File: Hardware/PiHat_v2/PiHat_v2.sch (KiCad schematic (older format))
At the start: 8 parts, among them P1 CONN_02X20, P2 CONN_01X02

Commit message: Correct EEPROM Schematic - Add Pin Numbers
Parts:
- PP1: footprint (none) -> Measurement_Points:Test_Point_2Pads
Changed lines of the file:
@@
 $EndComp
 $Comp
-L +3.3V #PWR1
+L +3.3V #PWR01
 U 1 1 588858F3
 P 1050 900
-F 0 "#PWR1" H 1050 750 50  0001 C CNN
+F 0 "#PWR01" H 1050 750 50  0001 C CNN
 F 1 "+3.3V" H 1050 1040 50  0000 C CNN
 F 2 "" H 1050 900 50  0000 C CNN
@@
 $EndComp
 $Comp
-L +5V #PWR3
+L +5V #PWR02
 U 1 1 58885909
 P 1700 900
-F 0 "#PWR3" H 1700 750 50  0001 C CNN
+F 0 "#PWR02" H 1700 750 50  0001 C CNN
 F 1 "+5V" H 1700 1040 50  0000 C CNN
 F 2 "" H 1700 900 50  0000 C CNN
@@
 $EndComp
 $Comp
-L GND #PWR4
+L GND #PWR03
 U 1 1 58885944
 P 1700 3100
-F 0 "#PWR4" H 1700 2850 50  0001 C CNN
+F 0 "#PWR03" H 1700 2850 50  0001 C CNN
 F 1 "GND" H 1700 2950 50  0000 C CNN
 F 2 "" H 1700 3100 50  0000 C CNN
@@
 $EndComp
 $Comp
-L GND #PWR2
+L GND #PWR04
 U 1 1 58885AD1
 P 1100 3100
-F 0 "#PWR2" H 1100 2850 50  0001 C CNN
+F 0 "#PWR04" H 1100 2850 50  0001 C CNN
 F 1 "GND" H 1100 2950 50  0000 C CNN
 F 2 "" H 1100 3100 50  0000 C CNN
@@
 ID_SD
 $Comp
-L GND #PWR5
+L GND #PWR05
 U 1 1 58887CDD
 P 2700 2300
-F 0 "#PWR5" H 2700 2050 50  0001 C CNN
+F 0 "#PWR05" H 2700 2050 50  0001 C CNN
 F 1 "GND" H 2700 2150 50  0000 C CNN
 F 2 "" H 2700 2300 50  0000 C CNN
@@
 $EndComp
 $Comp
-L +3.3V #PWR8
+L +3.3V #PWR06
 U 1 1 58887DFD
 P 3750 1250
-F 0 "#PWR8" H 3750 1100 50  0001 C CNN
+F 0 "#PWR06" H 3750 1100 50  0001 C CNN
 F 1 "+3.3V" H 3750 1390 50  0000 C CNN
 F 2 "" H 3750 1250 50  0000 C CNN
@@
 $EndComp
 $Comp
-L GND #PWR6
+L GND #PWR07
 U 1 1 58887E15
 P 3350 1500
-F 0 "#PWR6" H 3350 1250 50  0001 C CNN
+F 0 "#PWR07" H 3350 1250 50  0001 C CNN
 F 1 "GND" H 3350 1350 50  0000 C CNN
 F 2 "" H 3350 1500 50  0000 C CNN
@@
 $EndComp
 $Comp
-L GND #PWR7
+L GND #PWR08
 U 1 1 58887E2F
 P 3700 2900
-F 0 "#PWR7" H 3700 2650 50  0001 C CNN
+F 0 "#PWR08" H 3700 2650 50  0001 C CNN
 F 1 "GND" H 3700 2750 50  0000 C CNN
 F 2 "" H 3700 2900 50  0000 C CNN
@@
 F 0 "PP1" H 3460 2770 50  0000 C CNN
 F 1 "horizTest" H 3450 2520 50  0000 C CNN
-F 2 "" H 3310 2700 50  0000 C CNN
+F 2 "Measurement_Points:Test_Point_2Pads" H 3310 2700 50  0001 C CNN
 F 3 "" H 3310 2700 50  0000 C CNN
 	1    3450 2650

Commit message: Rough Sketch of Schematic and all Footprints Complete
* I've completed a first draft of the schematic, and verified that all
parts have a footprint.
* Next steps include routing the PCB, verifying the designs, and
including any changes.
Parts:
- added LED1: Led_RGB_CA, LEDs:LED_Cree-PLCC4, symbol Led_RGB_CA
- added P3: CONN_01X08, Pin_Headers:Pin_Header_Straight_1x08_Pitch2.54mm, symbol CONN_01X08
- added R4, R5, R6: R, Resistors_SMD:R_0805_HandSoldering, symbol R
- added S1: Piezo, .pretty:PKM13EPYH, symbol Piezo
- added aux1, aux2, aux3, aux4: CONN_01X02, Connectors_Molex:Molex_KK-6410-02_02x2.54mm_Straight, symbol CONN_01X02
- added temp1: LM75BD, Housings_SOIC:SOIC-8_3.9x4.9mm_Pitch1.27mm, symbol LM75BD
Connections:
- wire segments 66 -> 94
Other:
- note added: "3x4 Keypad"
- note added: "Aux Switch Connections"
- note added: "Piezo Buzzer"
- note added: "RGB Led - Common Anode"
- note added: "i2c Temperature Sensor"
- moved on the sheet: C1, ID_EEPROM1, P1, P2, PP1, R1, R2, R3

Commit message: Merge branch 'clemsonMakerspace/devel' into devel
# Conflicts:
#	Software/scan_key/AuthenticationSQL.py
#	Software/scan_key/main.py
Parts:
- removed LED1: Led_RGB_CA, LEDs:LED_Cree-PLCC4, symbol Led_RGB_CA
- removed R4, R5, R6: R, Resistors_SMD:R_0805_HandSoldering, symbol R
- added C2: 100n, Capacitors_SMD:C_0805_HandSoldering, symbol C
- added D1: D_Schottky, .pretty:Schottky_Diode, symbol D_Schottky
- added P4: Neo_LED_RGB_IC, .pretty:Neo_RGB_LED, symbol Neo_LED_RGB_IC
- added aux5: CONN_01X02, Connectors_Molex:Molex_KK-6410-02_02x2.54mm_Straight, symbol CONN_01X02
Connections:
- wire segments 94 -> 93
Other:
- note added: "RGB Neopixel Led - Integrated IC"
- note removed: "RGB Led - Common Anode"
- moved on the sheet: C1, ID_EEPROM1, P1, P2, P3, PP1, R1, R2, R3, S1, aux1, aux2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

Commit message: Merge remote-tracking branch 'refs/remotes/clemsonMakerspace/devel' into devel
# Conflicts:
#	Hardware/PiHat_v2/.pretty/Neo_RGB_LED.kicad_mod
#	Hardware/PiHat_v2/PiHat_v2.kicad_pcb
#	Hardware/PiHat_v2/PiHat_v2.kicad_pcb-bak
#	Hardware/PiHat_v2/PiHat_v2.net
#	Hardware/PiHat_v2/PiHat_v2.pro
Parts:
- removed D1: D_Schottky, .pretty:Schottky_Diode, symbol D_Schottky
- added ATMEGA1: ATMEGA328P-A, .pretty:ATMEGA328P, symbol ATMEGA328P-A
- added C3, C4: 20p, Capacitors_THT:C_Disc_D5.0mm_W2.5mm_P2.50mm, symbol C
- added OSC1: 16 MHz Crystal, Crystals:Resonator-2pin_w10.0mm_h5.0mm, symbol Piezo
- added R4: 1K, Resistors_SMD:R_0805_HandSoldering, symbol R
- added R5: 10K, Resistors_SMD:R_0805_HandSoldering, symbol R
- P3: footprint Pin_Headers:Pin_Header_Straight_1x08_Pitch2.54mm -> .pretty:Keypad_Ethernet
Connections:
- net labels added: ADC6, PB1, PD3, PD6, UART_RXD, UART_TXD
- net labels removed: GPIO14, GPIO15
- wire segments 93 -> 120
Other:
- note added: "Second Microcontroller\n"
- moved on the sheet: C1, ID_EEPROM1, P2, PP1, R1, R2, R3, S1, temp1

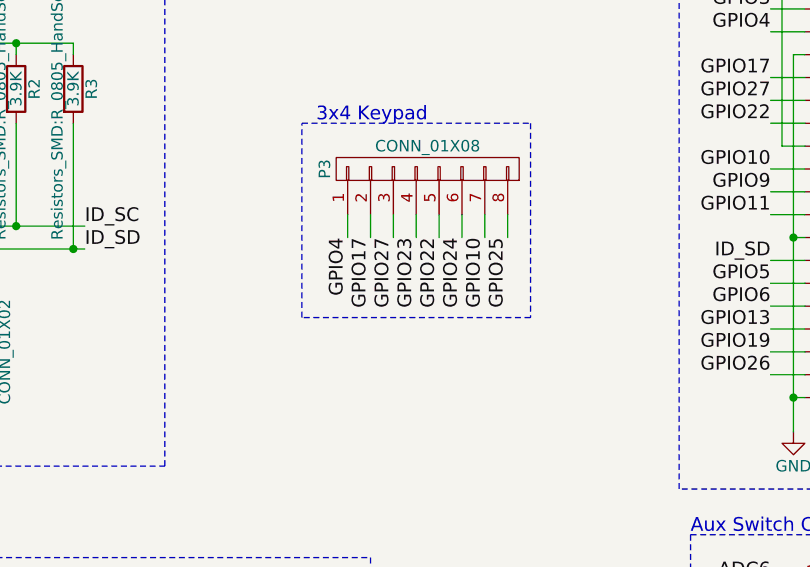
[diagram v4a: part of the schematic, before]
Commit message: Fixed my branch and moved ethernet port
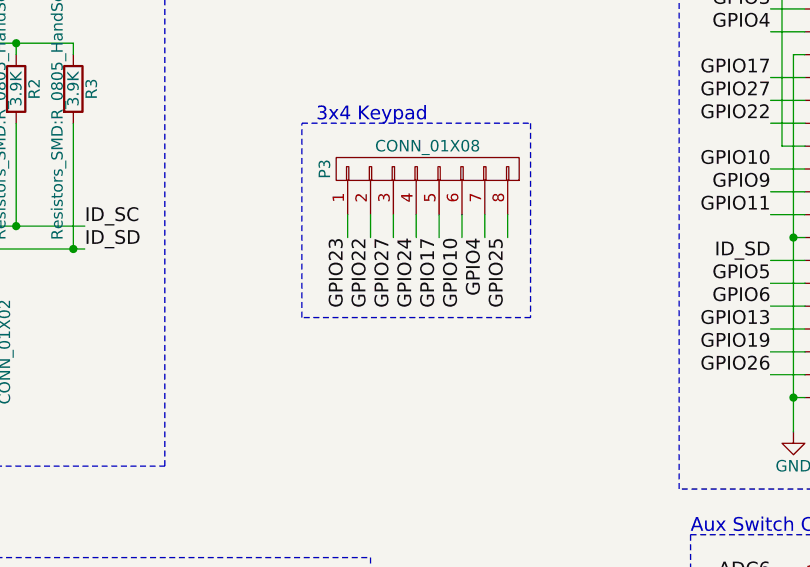
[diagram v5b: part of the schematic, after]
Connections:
- net GPIO10: now also P3.6 (P6); no longer P3.7 (P7)
- net GPIO17: now also P3.5 (P5); no longer P3.2 (P2)
- net GPIO22: now also P3.2 (P2); no longer P3.5 (P5)
- net GPIO23: now also P3.1 (P1); no longer P3.4 (P4)
- net GPIO24: now also P3.4 (P4); no longer P3.6 (P6)
- net GPIO4: now also P3.7 (P7); no longer P3.1 (P1)
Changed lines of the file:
@@
 Text Label 2150 1400 2    60   ~ 0
 PB1
-Text Label 6550 2950 3    60   ~ 0
+Text Label 7150 2950 3    60   ~ 0
 GPIO4
-Text Label 6650 2950 3    60   ~ 0
+Text Label 6950 2950 3    60   ~ 0
 GPIO17
 Text Label 6750 2950 3    60   ~ 0
 GPIO27
-Text Label 6850 2950 3    60   ~ 0
+Text Label 6550 2950 3    60   ~ 0
 GPIO23
 Wire Wire Line
 	7250 2850 7250 2950
-Text Label 6950 2950 3    60   ~ 0
+Text Label 6650 2950 3    60   ~ 0
 GPIO22
+Text Label 6850 2950 3    60   ~ 0
+GPIO24
 Text Label 7050 2950 3    60   ~ 0
-GPIO24
-Text Label 7150 2950 3    60   ~ 0
 GPIO10
 Text Label 7250 2950 3    60   ~ 0

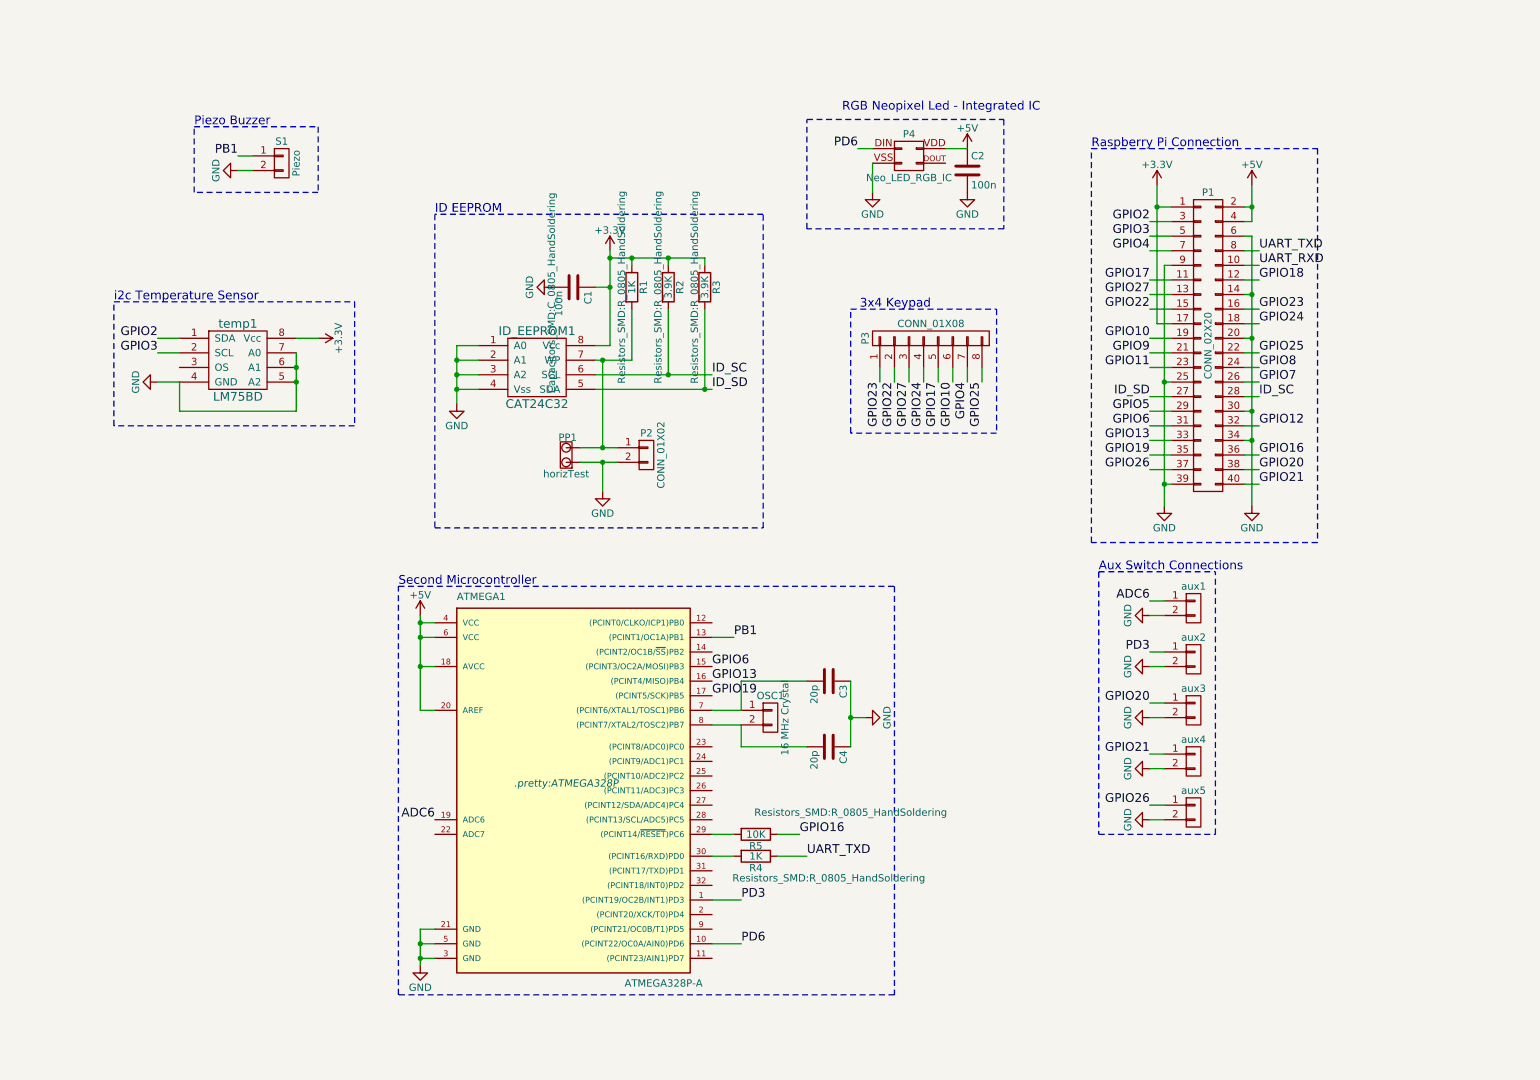
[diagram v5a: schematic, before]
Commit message: Schematic for Neopixel Chain & ISP Program Header
I've chained 5 Neopixels and added an ISP header for the ATMEGA.
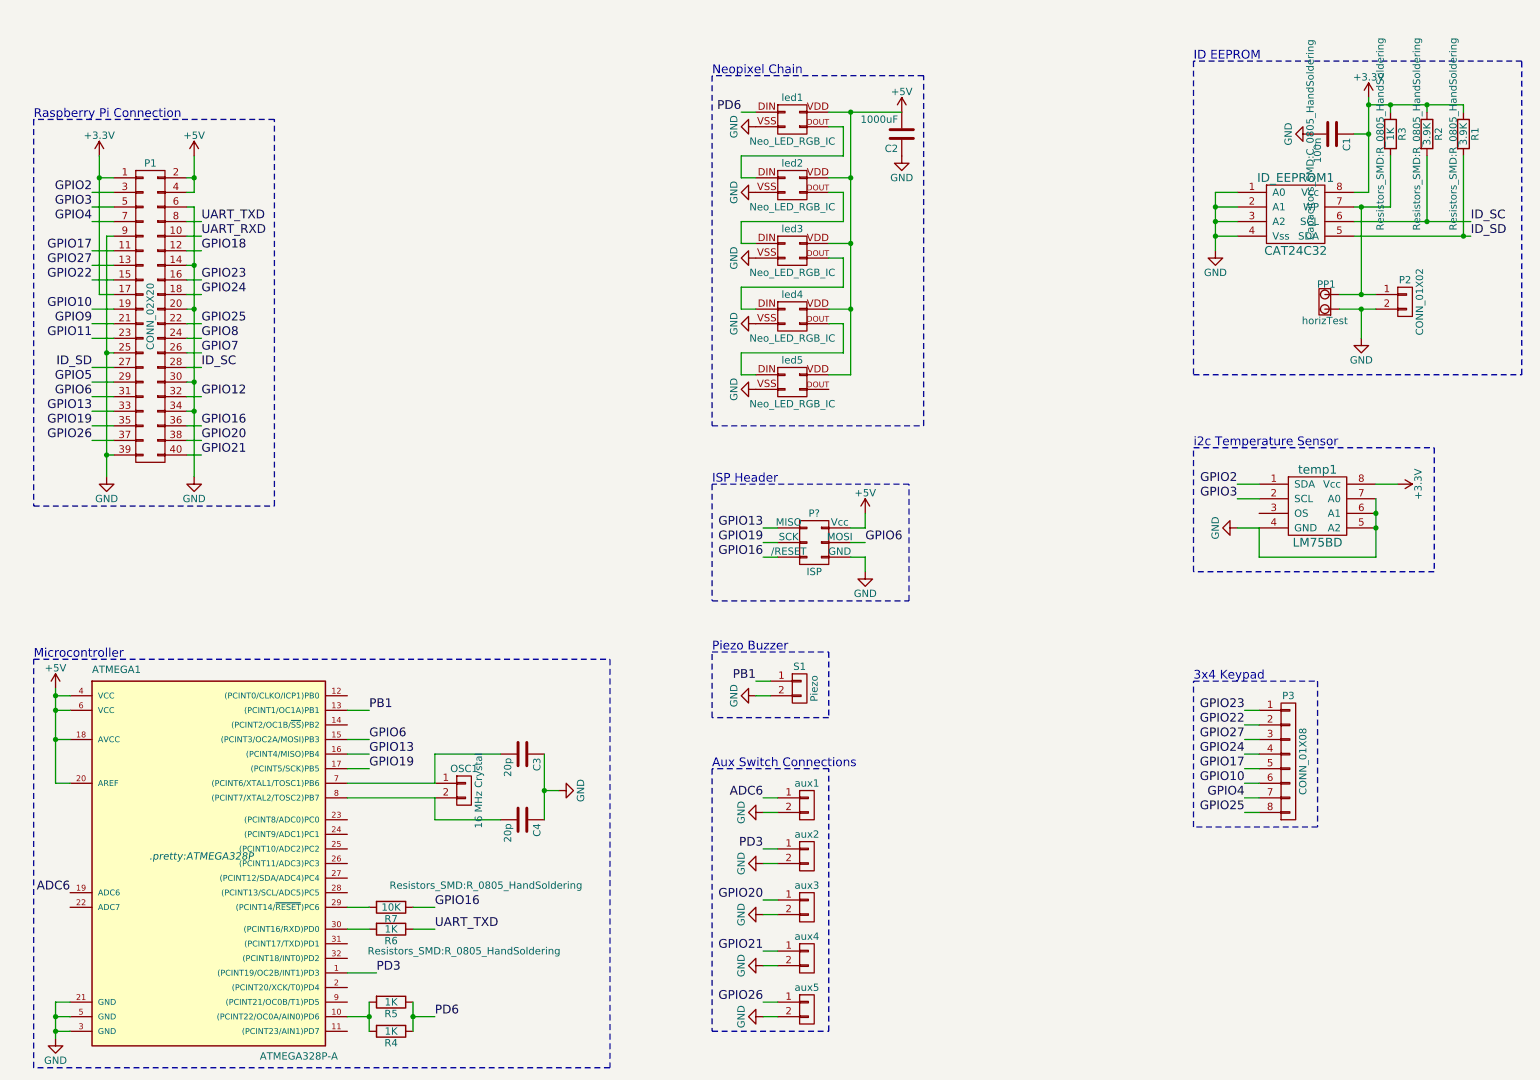
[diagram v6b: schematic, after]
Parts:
- added P?: ISP, symbol ISP
- added R4, R5: 1K, symbol R
- added led2, led3, led4, led5: Neo_LED_RGB_IC, .pretty:Neo_RGB_LED, symbol Neo_LED_RGB_IC
- C2: value 100n -> 1000uF
- renumbered R3 to R1, R1 to R3, R4 to R6, R5 to R7, P4 to led1
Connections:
- net +5V: now also C2.2, P?.2 (Vcc), led2.VDD, led3.VDD, led4.VDD, led5.VDD; no longer C2.1
- net GND: now also C2.1, P?.6 (GND), led2.VSS, led3.VSS, led4.VSS, led5.VSS; no longer C2.2
- net GPIO13: now also P?.1 (MISO)
- net GPIO16: now also P?.5 (/RESET)
- net GPIO19: now also P?.3 (SCK)
- net GPIO6: now also P?.4 (MOSI)
- net PD6: now also R4.1, R5.1; no longer ATMEGA1.10 ((PCINT22/OC0A/AIN0)PD6)
- net at led1.DOUT: now also led2.DIN
- new net: ATMEGA1.10 ((PCINT22/OC0A/AIN0)PD6), R4.2, R5.2
- new net: led2.DOUT, led3.DIN
- new net: led3.DOUT, led4.DIN
- new net: led4.DOUT, led5.DIN
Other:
- note added: "ISP Header"
- note added: "Microcontroller\n"
- note added: "Neopixel Chain"
- note removed: "RGB Neopixel Led - Integrated IC"
- note removed: "Second Microcontroller\n"
- moved on the sheet: ATMEGA1, C1, C2, C3, C4, ID_EEPROM1, OSC1, P1, P2, P3, PP1, R1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

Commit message: Add PWR_FLAG to Schematic
Solves "Pin connected to some other pins but no pin to drive it ERC
error.
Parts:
- gave numbers to parts that had none: 1
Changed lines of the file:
@@
 GPIO13
 $Comp
-L +5V #PWR?
+L +5V #PWR027
 U 1 1 5945B2FD
 P 6450 3850
-F 0 "#PWR?" H 6450 3700 50  0001 C CNN
+F 0 "#PWR027" H 6450 3700 50  0001 C CNN
 F 1 "+5V" H 6450 3990 50  0000 C CNN
 F 2 "" H 6450 3850 50  0000 C CNN
@@
 $EndComp
 $Comp
-L GND #PWR?
+L GND #PWR028
 U 1 1 5945B34F
 P 6450 4250
-F 0 "#PWR?" H 6450 4000 50  0001 C CNN
+F 0 "#PWR028" H 6450 4000 50  0001 C CNN
 F 1 "GND" H 6450 4100 50  0000 C CNN
 F 2 "" H 6450 4250 50  0000 C CNN
@@
 $EndComp
 $Comp
-L ISP P?
+L ISP ISP1
 U 1 1 594627ED
 P 6100 4050
-F 0 "P?" H 6100 4250 50  0000 C CNN
+F 0 "ISP1" H 6100 4250 50  0000 C CNN
 F 1 "ISP" H 6100 3850 50  0000 C CNN
 F 2 "" H 6100 2850 50  0000 C CNN
@@
 Wire Notes Line
 	750  1150 750  3800
+$Comp
+L +5V #PWR029
+U 1 1 5946A3FE
+P 3200 1150
+F 0 "#PWR029" H 3200 1000 50  0001 C CNN
+F 1 "+5V" H 3200 1290 50  0000 C CNN
+F 2 "" H 3200 1150 50  0000 C CNN
+F 3 "" H 3200 1150 50  0000 C CNN
+	1    3200 1150
+	1    0    0    -1
+$EndComp
+$Comp
+L GND #PWR030
+U 1 1 5946A450
+P 3600 1150
+F 0 "#PWR030" H 3600 900 50  0001 C CNN
+F 1 "GND" H 3600 1000 50  0000 C CNN
+F 2 "" H 3600 1150 50  0000 C CNN
+F 3 "" H 3600 1150 50  0000 C CNN
+	1    3600 1150
+	-1   0    0    1
+$EndComp
+$Comp
+L PWR_FLAG #FLG031
+U 1 1 5946A549
+P 3200 1350
+F 0 "#FLG031" H 3200 1445 50  0001 C CNN
+F 1 "PWR_FLAG" H 3200 1530 50  0000 C CNN
+F 2 "" H 3200 1350 50  0000 C CNN
+F 3 "" H 3200 1350 50  0000 C CNN
+	1    3200 1350
+	-1   0    0    1
+$EndComp
+$Comp
+L PWR_FLAG #FLG032
+U 1 1 5946A59B
+P 3600 1350
+F 0 "#FLG032" H 3600 1445 50  0001 C CNN
+F 1 "PWR_FLAG" H 3600 1530 50  0000 C CNN
+F 2 "" H 3600 1350 50  0000 C CNN
+F 3 "" H 3600 1350 50  0000 C CNN
+	1    3600 1350
+	-1   0    0    1
+$EndComp
+Wire Wire Line
+	3200 1150 3200 1350
+Wire Wire Line
+	3600 1150 3600 1350
 $EndSCHEMATC
